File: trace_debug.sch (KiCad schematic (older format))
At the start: 7 parts

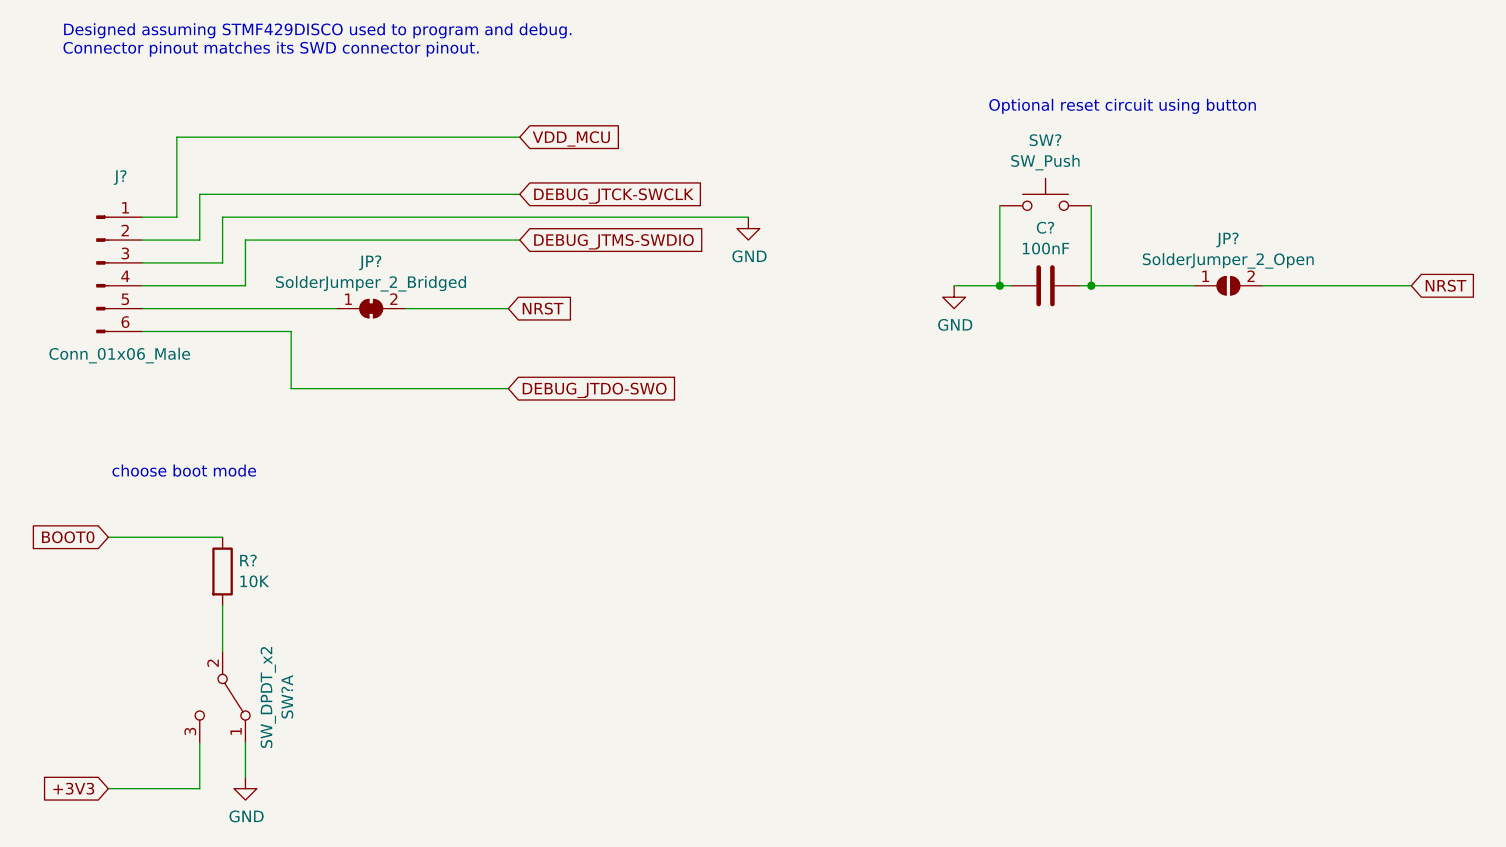
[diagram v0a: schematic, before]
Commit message: First proposed pin layout of SODIMM connector
Will need to add GPIO / ADC pins as needed, but let's wait to see if we don't
need to use more pins.

Double-checked and fixed CODEC and MCU's power supply.
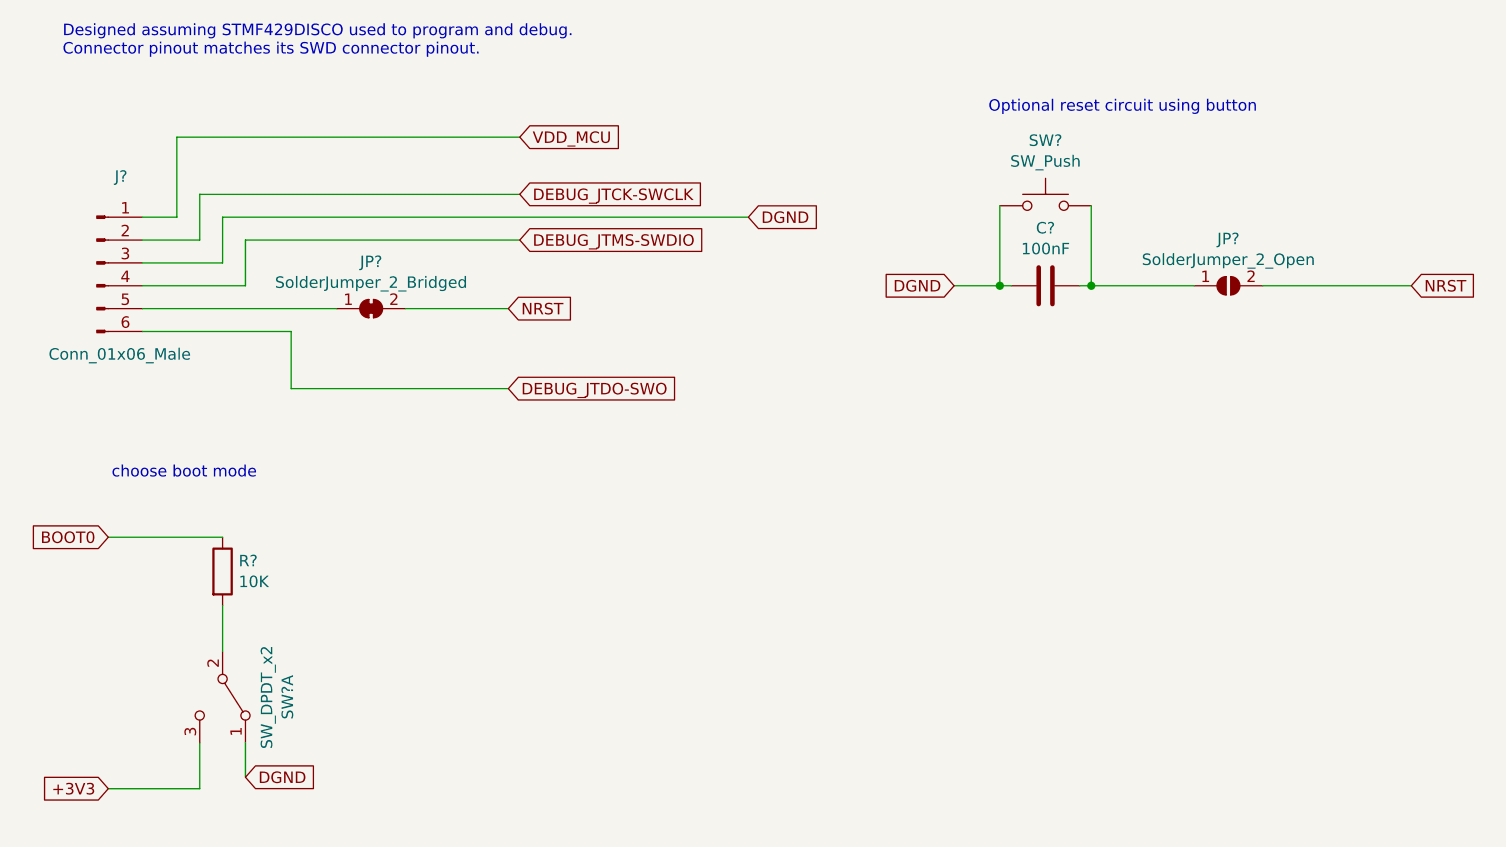
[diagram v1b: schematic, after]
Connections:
- net GND renamed DGND
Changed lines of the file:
@@
 $Descr A4 11693 8268
 encoding utf-8
-Sheet 5 12
+Sheet 5 13
 Title ""
 Date ""
@@
 Wire Wire Line
 	6900 1800 6250 1800
-$Comp
-L power:GND #PWR?
-U 1 1 5CF60A37
-P 4900 1800
-F 0 "#PWR?" H 4900 1550 50  0001 C CNN
-F 1 "GND" H 4905 1627 50  0000 C CNN
-F 2 "" H 4900 1800 50  0001 C CNN
-F 3 "" H 4900 1800 50  0001 C CNN
-	1    4900 1800
-	1    0    0    -1
-$EndComp
 Wire Wire Line
 	5100 1450 5100 1800
@@
 Wire Wire Line
 	1800 1600 3000 1600
-$Comp
-L power:GND #PWR?
-U 1 1 5CF61324
-P 4000 1500
-F 0 "#PWR?" H 4000 1250 50  0001 C CNN
-F 1 "GND" H 4005 1327 50  0000 C CNN
-F 2 "" H 4000 1500 50  0001 C CNN
-F 3 "" H 4000 1500 50  0001 C CNN
-	1    4000 1500
-	1    0    0    -1
-$EndComp
 Wire Wire Line
 	1350 1700 1700 1700
@@
 Wire Wire Line
 	1700 3200 1700 3400
-$Comp
-L power:GND #PWR?
-U 1 1 5CF687C3
-P 1800 3950
-F 0 "#PWR?" H 1800 3700 50  0001 C CNN
-F 1 "GND" H 1805 3777 50  0000 C CNN
-F 2 "" H 1800 3950 50  0001 C CNN
-F 3 "" H 1800 3950 50  0001 C CNN
-	1    1800 3950
-	1    0    0    -1
-$EndComp
 Wire Wire Line
 	1800 3800 1800 3950
@@
 Wire Wire Line
 	1200 4000 1600 4000
+Text GLabel 4900 1800 0    50   Input ~ 0
+DGND
+Text GLabel 4000 1500 2    50   Input ~ 0
+DGND
+Text GLabel 1800 3950 2    50   Input ~ 0
+DGND
 $EndSCHEMATC
